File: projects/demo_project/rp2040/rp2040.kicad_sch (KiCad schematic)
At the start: 36 parts, among them J1 USB_C_Receptacle, J2 TC2030-IDC-NL, SW1 PTS815, U1 RP2040, U2 W25Q16JV, U3 TPS63051, U4 SHT40-AD1B, Y1 CSTNE12M0GH5L000R0

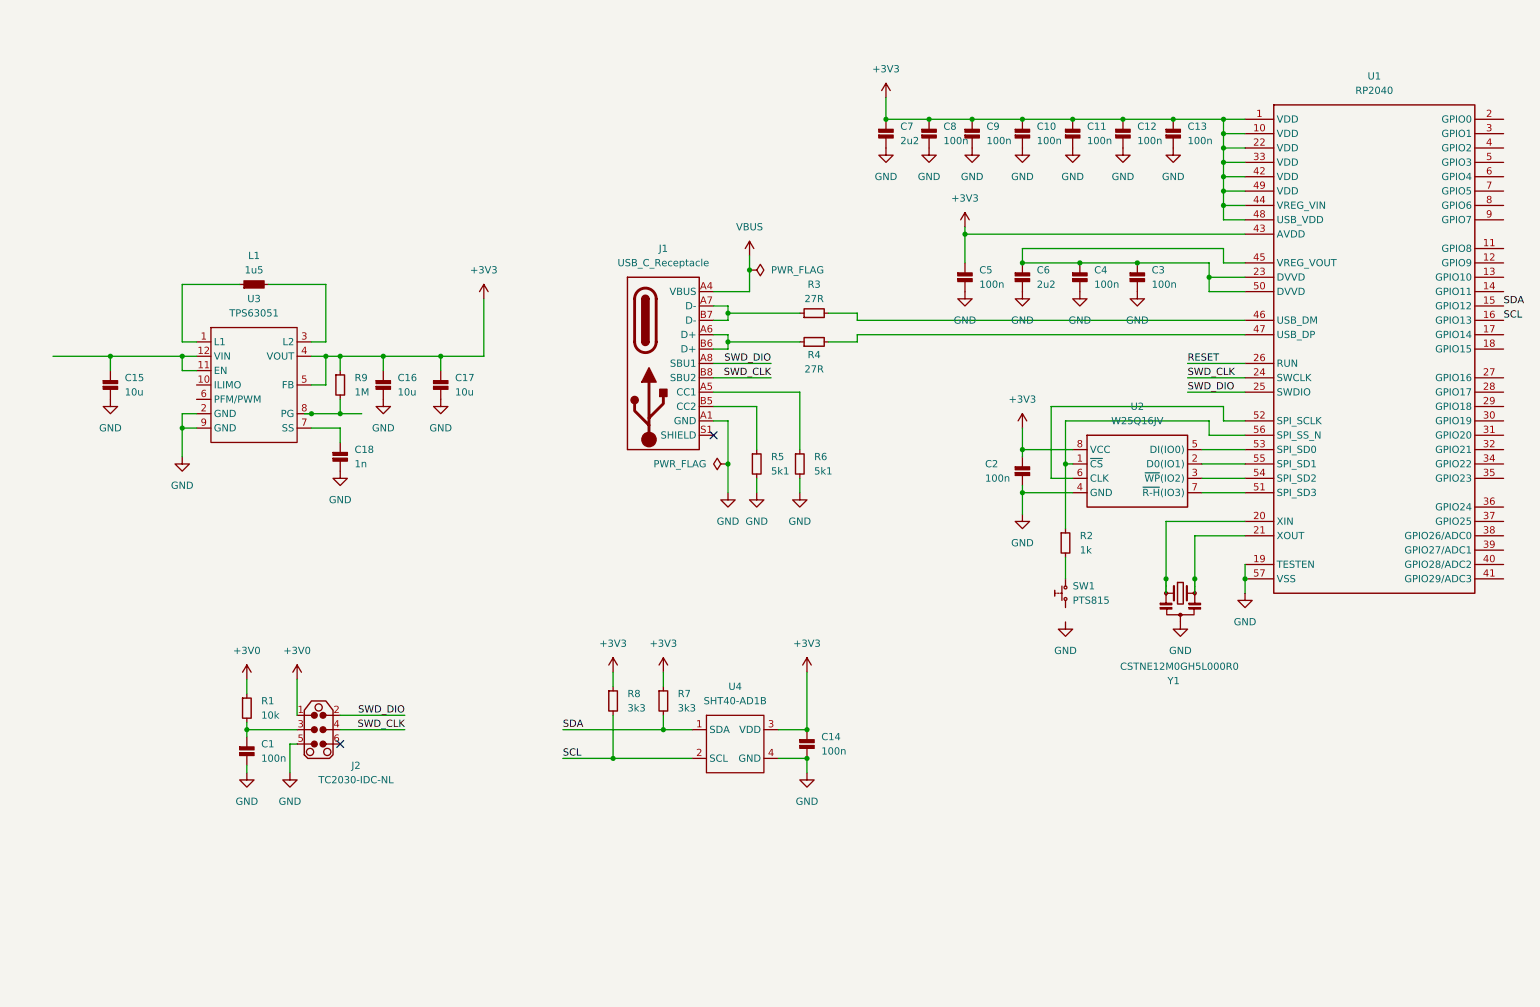
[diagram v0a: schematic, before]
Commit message: finish schematic and route gpio traces
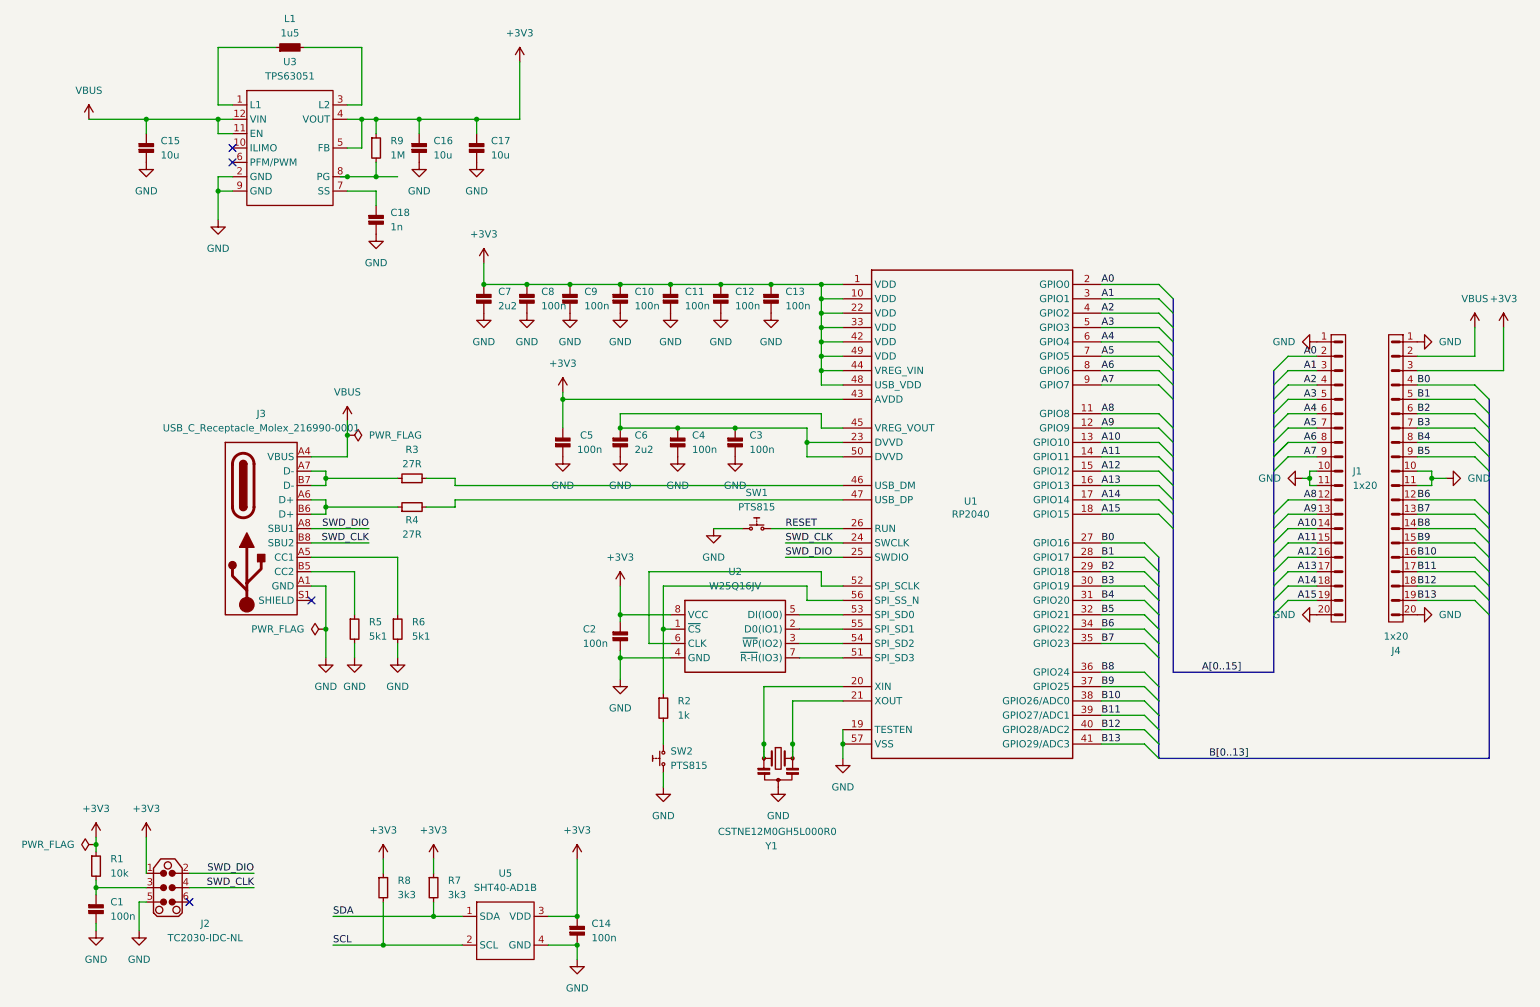
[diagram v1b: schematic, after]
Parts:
- removed J1: USB_C_Receptacle, symbol connector:USB_C_Receptacle
- removed U4: SHT40-AD1B, none, symbol db:ic/26.000.0017
- added J1, J4: 1x20, connector:PinHeader_1x20_P2.54mm_Vertical, symbol db:connector/12.000.0022
- added J3: USB_C_Receptacle_Molex_216990-0001, connector:USB_C_Receptacle_MidMnt_Molex_16_Contact_216990-0001, symbol db:connector/12.010.001
- added SW2: PTS815, switch:TS02-66-Series, symbol db:switch/23.000.0016
- added U5: SHT40-AD1B, ic:Sensirion_DFN-4_1.5x1.5mm_P0.8mm_SHT4x_NoCentralPad, symbol db:ic/26.000.0017
- L1: footprint passive:L_3.2mmx2.5mm -> passive:L_3.2x2.5; FP L_3.2mmx2.5mm -> L_3.2x2.5; Modified 2024-02-14 19:30:12 -> 2025-02-13 12:54:55; Version 0 -> 1
- SW1: footprint none -> switch:TS02-66-Series; FP none -> TS02-66-Series; Modified 2025-02-12 12:22:43 -> 2025-02-13 12:47:32; Version 4 -> 5
- U3: footprint I -> package:VQFN-12-1EP_2.5x2.5mm_P0.5mm; FP I -> VQFN-12-1EP_2.5x2.5mm_P0.5mm; Modified 2025-02-12 13:26:04 -> 2025-02-13 13:06:41; Version 2 -> 4
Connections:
- net +3V0 is gone; now on net +3V3: J2.1, R1.1
- net +3V3: now also J4.3, U5.3 (VDD)
- net GND: now also SW1.1, J1.1, J1.10, J1.11, J1.20, J3.A1 (GND), J3.A12 (GND), J3.B1 (GND), J3.B12 (GND), J4.1, J4.10, J4.11, J4.20, SW2.1, U5.4 (GND)
- net RESET: now also SW1.2
- net SCL: now also U5.2 (SCL); no longer U1.16 (GPIO13)
- net SDA: now also U5.1 (SDA); no longer U1.15 (GPIO12)
- net SWD_CLK: now also J3.B8 (SBU2)
- net SWD_DIO: now also J3.A8 (SBU1)
- net VBUS: now also C15.1, U3.11 (EN), U3.12 (VIN), J3.A4 (VBUS), J3.A9 (VBUS), J3.B4 (VBUS), J3.B9 (VBUS), J4.2
- net at R5.1: now also J3.B5 (CC2)
- net at R6.1: now also J3.A5 (CC1)
- net at R4.1: now also J3.A6 (D+), J3.B6 (D+)
- net at R3.1: now also J3.A7 (D-), J3.B7 (D-)
- net A8: now reaches U1.11 (GPIO8)
- net A8: now also J1.12
- net A9: now reaches U1.12 (GPIO9)
- net A9: now also J1.13
- net A10: now reaches U1.13 (GPIO10)
- net A10: now also J1.14
- net A11: now reaches U1.14 (GPIO11)
- net A11: now also J1.15
- net A14: now reaches U1.17 (GPIO14)
- net A14: now also J1.18
- net A15: now reaches U1.18 (GPIO15)
- net A15: now also J1.19
- net A0: now reaches U1.2 (GPIO0)
- net A0: now also J1.2
- net B0: now reaches U1.27 (GPIO16)
- net B0: now also J4.4
- net B1: now reaches U1.28 (GPIO17)
- net B1: now also J4.5
- net B2: now reaches U1.29 (GPIO18)
- net B2: now also J4.6
- net A1: now reaches U1.3 (GPIO1)
- net A1: now also J1.3
- net B3: now reaches U1.30 (GPIO19)
- net B3: now also J4.7
- net B4: now reaches U1.31 (GPIO20)
- net B4: now also J4.8
- net B5: now reaches U1.32 (GPIO21)
- net B5: now also J4.9
- net B6: now reaches U1.34 (GPIO22)
- net B6: now also J4.12
- net B7: now reaches U1.35 (GPIO23)
- net B7: now also J4.13
- net B8: now reaches U1.36 (GPIO24)
- net B8: now also J4.14
- net B9: now reaches U1.37 (GPIO25)
- net B9: now also J4.15
- net B10: now reaches U1.38 (GPIO26/ADC0)
- net B10: now also J4.16
- net B11: now reaches U1.39 (GPIO27/ADC1)
- net B11: now also J4.17
- net A2: now reaches U1.4 (GPIO2)
- net A2: now also J1.4
- net B12: now reaches U1.40 (GPIO28/ADC2)
- net B12: now also J4.18
- net B13: now reaches U1.41 (GPIO29/ADC3)
- net B13: now also J4.19
- net A3: now reaches U1.5 (GPIO3)
- net A3: now also J1.5
- net A4: now reaches U1.6 (GPIO4)
- net A4: now also J1.6
- net A5: now reaches U1.7 (GPIO5)
- net A5: now also J1.7
- net A6: now reaches U1.8 (GPIO6)
- net A6: now also J1.8
- net A7: now reaches U1.9 (GPIO7)
- net A7: now also J1.9
- net at R2.2: now also SW2.2; no longer SW1.2
- new net A12: J1.16, U1.15 (GPIO12)
- new net A13: J1.17, U1.16 (GPIO13)
- no-connect marks 2 -> 4
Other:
- moved on the sheet: C1, C10, C11, C12, C13, C14, C15, C16, C17, C18, C2, C3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

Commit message: finish layout
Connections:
- net USB_P: now reaches J3.A6 (D+), J3.B6 (D+), R4.1
- net USB_N: now reaches J3.A7 (D-), J3.B7 (D-), R3.1
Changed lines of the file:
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@@
+		)
+	)
+	(label "USB_N"
+		(at 69.85 95.25 0)
+		(fields_autoplaced yes)
+		(effects
+			(font
+				(size 1.27 1.27)
+			)
+			(justify left bottom)
+		)
+		(property "Netclass" "USB"
+			(at 69.85 96.52 0)
+			(effects
+				(font
+					(size 1.27 1.27)
+					(italic yes)
+				)
+				(justify left)
+				(hide yes)
+			)
 		)
 	)
@@
 		)
 	)
+	(label "USB_P"
+		(at 69.85 100.33 0)
+		(fields_autoplaced yes)
+		(effects
+			(font
+				(size 1.27 1.27)
+			)
+			(justify left bottom)
+		)
+		(property "Netclass" "USB"
+			(at 69.85 101.6 0)
+			(effects
+				(font
+					(size 1.27 1.27)
+					(italic yes)
+				)
+				(justify left)
+				(hide yes)
+			)
+		)
+	)
